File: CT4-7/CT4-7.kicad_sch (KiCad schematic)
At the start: 26 parts

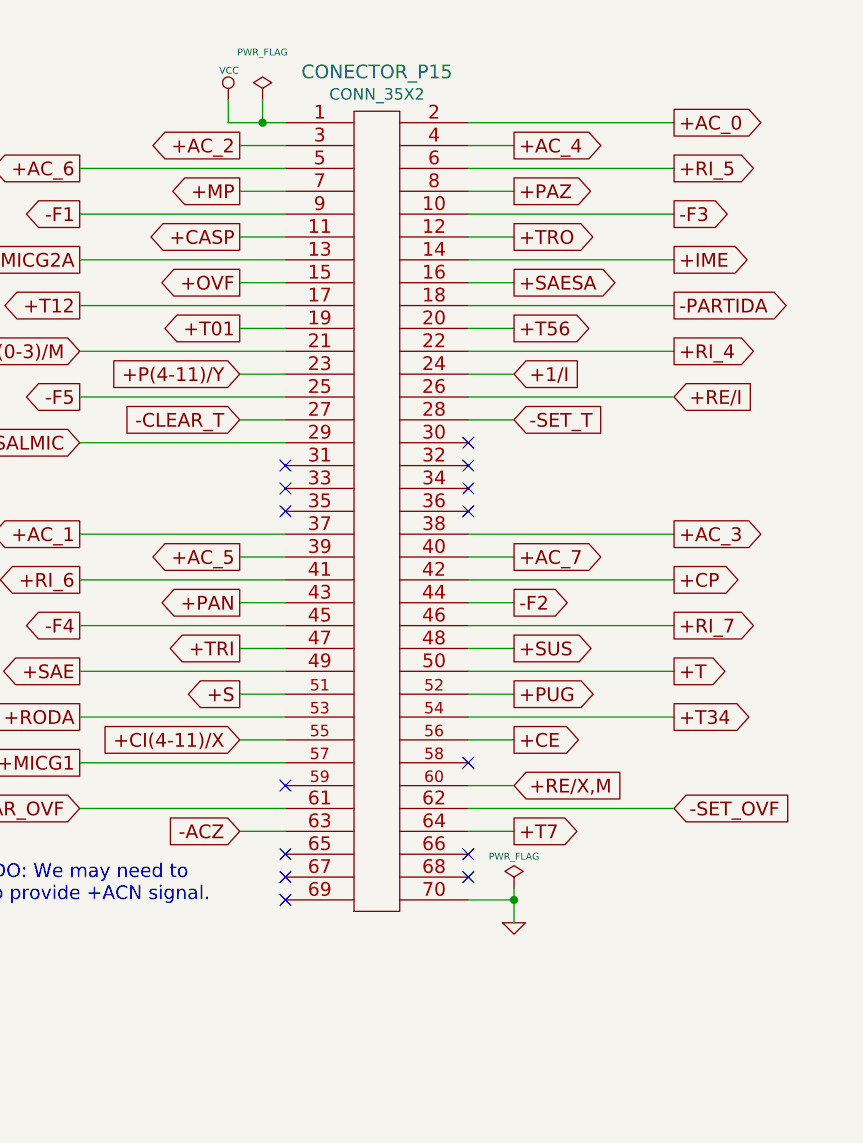
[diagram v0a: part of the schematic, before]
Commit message: cleaning up references
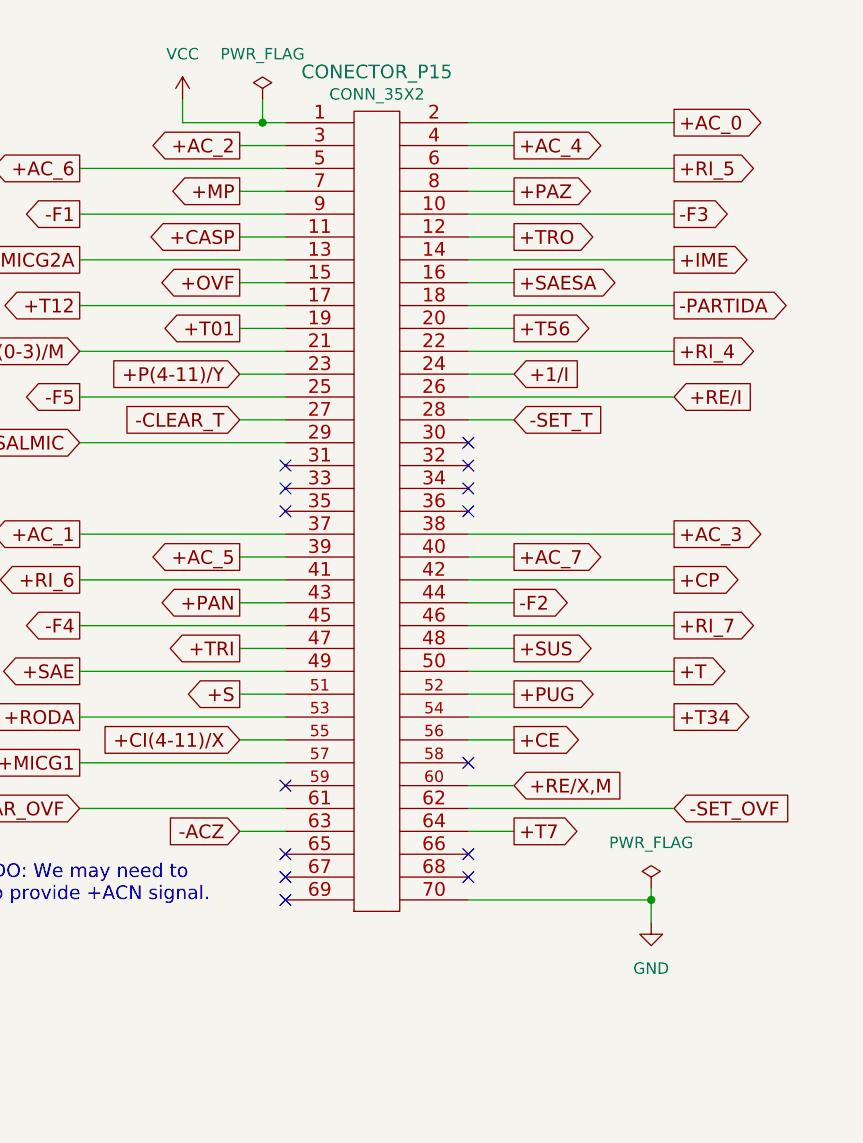
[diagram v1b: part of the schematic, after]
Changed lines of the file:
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@@
 	)
 	(junction
-		(at 472.44 215.9)
+		(at 160.02 213.36)
 		(diameter 0)
 		(color 0 0 0 0)
 	)
 	(junction
-		(at 472.44 210.82)
+		(at 472.44 215.9)
 		(diameter 0)
 		(color 0 0 0 0)
 	)
 	(junction
-		(at 499.11 392.43)
+		(at 472.44 210.82)
 		(diameter 0)
 		(color 0 0 0 0)
 	)
 	(junction
-		(at 538.48 430.53)
+		(at 499.11 392.43)
 		(diameter 0)
 		(color 0 0 0 0)
 	)
 	(junction
-		(at 144.78 213.36)
+		(at 538.48 430.53)
 		(diameter 0)
 		(color 0 0 0 0)
@@
 	(wire
 		(pts
-			(xy 139.7 213.36) (xy 144.78 213.36)
+			(xy 139.7 213.36) (xy 160.02 213.36)
 		)
 		(stroke
@@
 	(wire
 		(pts
-			(xy 144.78 212.09) (xy 144.78 213.36)
+			(xy 160.02 212.09) (xy 160.02 213.36)
 		)
 		(stroke
@@
 	(wire
 		(pts
-			(xy 113.03 127) (xy 116.84 127)
+			(xy 107.95 127) (xy 116.84 127)
 		)
 		(stroke
@@
 	(wire
 		(pts
-			(xy 144.78 213.36) (xy 144.78 215.9)
+			(xy 160.02 213.36) (xy 160.02 215.9)
 		)
 		(stroke
@@
 	(wire
 		(pts
-			(xy 113.03 127) (xy 113.03 124.46)
+			(xy 107.95 127) (xy 107.95 124.46)
 		)
 		(stroke
@@
 	)
 	(symbol
-		(lib_id "CT4-7-rescue:PWR_FLAG-power")
-		(at 116.84 124.46 0)
+		(lib_id "power:GND")
+		(at 160.02 215.9 0)
 		(unit 1)
 		(body_style 1)
@@
 		(in_pos_files yes)
 		(dnp no)
-		(property "Reference" "#FLG01"
-			(at 116.84 122.047 0)
+		(fields_autoplaced yes)
+		(property "Reference" "#PWR0137"
+			(at 160.02 222.25 0)
 			(hide yes)
 			(show_name no)
@@
 			(effects
 				(font
-					(size 0.762 0.762)
+					(size 1.27 1.27)
 				)
 			)
 		)
-		(property "Value" "PWR_FLAG"
-			(at 116.84 119.1768 0)
+		(property "Value" "GND"
+			(at 160.02 220.98 0)
 			(show_name no)
 			(do_not_autoplace no)
 			(effects
 				(font
-					(size 0.762 0.762)
+					(size 1.27 1.27)
 				)
 			)
 		)
 		(property "Footprint" ""
-			(at 116.84 124.46 0)
+			(at 160.02 215.9 0)
 			(hide yes)
 			(show_name no)
@@
 			(effects
 				(font
-					(size 1.524 1.524)
+					(size 1.27 1.27)
 				)
 			)
 		)
 		(property "Datasheet" ""
-			(at 116.84 124.46 0)
+			(at 160.02 215.9 0)
 			(hide yes)
 			(show_name no)
@@
 			(effects
 				(font
-					(size 1.524 1.524)
+					(size 1.27 1.27)
 				)
 			)
 		)
-		(property "Description" ""
-			(at 116.84 124.46 0)
+		(property "Description" "Power symbol creates a global label with name \"GND\" , ground"
+			(at 160.02 215.9 0)
+			(hide yes)
 			(show_name no)
 			(do_not_autoplace no)
@@
 		)
 		(instances
-			(project ""
-				(path "/91180d67-5efd-47f3-b787-983030024d4a"
-					(reference "#FLG01")
-					(unit 1)
-				)
-			)
 			(project "patinhofeio"
 				(path "/aca06203-542d-4682-a7e3-8839e24cce95/20195246-952b-457f-8d3f-2119f4e5893d"
-					(reference "#FLG01")
+					(reference "#PWR0137")
 					(unit 1)
 				)
@@
 	)
 	(symbol
-		(lib_id "CT4-7-rescue:VCC-power")
-		(at 113.03 124.46 0)
+		(lib_id "power:PWR_FLAG")
+		(at 116.84 124.46 0)
 		(unit 1)
 		(body_style 1)
@@
 		(in_pos_files yes)
 		(dnp no)
-		(property "Reference" "#PWR02"
-			(at 113.03 121.92 0)
+		(fields_autoplaced yes)
+		(property "Reference" "#FLG058"
+			(at 116.84 122.555 0)
 			(hide yes)
 			(show_name no)
@@
 			(effects
 				(font
-					(size 0.762 0.762)
+					(size 1.27 1.27)
 				)
 			)
 		)
-		(property "Value" "VCC"
-			(at 113.1062 121.2088 0)
+		(property "Value" "PWR_FLAG"
+			(at 116.84 119.38 0)
 			(show_name no)
 			(do_not_autoplace no)
 			(effects
 				(font
-					(size 0.762 0.762)
+					(size 1.27 1.27)
 				)
 			)
 		)
 		(property "Footprint" ""
-			(at 113.03 124.46 0)
+			(at 116.84 124.46 0)
 			(hide yes)
 			(show_name no)
@@
 			(effects
 				(font
-					(size 1.524 1.524)
+					(size 1.27 1.27)
 				)
 			)
 		)
 		(property "Datasheet" ""
-			(at 113.03 124.46 0)
+			(at 116.84 124.46 0)
 			(hide yes)
 			(show_name no)
@@
 			(effects
 				(font
-					(size 1.524 1.524)
+					(size 1.27 1.27)
 				)
 			)
 		)
-		(property "Description" ""
-			(at 113.03 124.46 0)
+		(property "Description" "Special symbol for telling ERC where power comes from"
+			(at 116.84 124.46 0)
+			(hide yes)
 			(show_name no)
 			(do_not_autoplace no)
@@
 		)
 		(instances
-			(project ""
-				(path "/91180d67-5efd-47f3-b787-983030024d4a"
-					(reference "#PWR02")
-					(unit 1)
-				)
-			)
 			(project "patinhofeio"
 				(path "/aca06203-542d-4682-a7e3-8839e24cce95/20195246-952b-457f-8d3f-2119f4e5893d"
-					(reference "#PWR02")
+					(reference "#FLG058")
 					(unit 1)
 				)
@@
 	)
 	(symbol
-		(lib_id "CT4-7-rescue:PWR_FLAG-power")
-		(at 144.78 212.09 0)
+		(lib_id "power:VCC")
+		(at 107.95 124.46 0)
 		(unit 1)
 		(body_style 1)
@@
 		(in_pos_files yes)
 		(dnp no)
-		(property "Reference" "#FLG03"
-			(at 144.78 209.677 0)
+		(fields_autoplaced yes)
+		(property "Reference" "#PWR0111"
+			(at 107.95 128.27 0)
 			(hide yes)
 			(show_name no)
@@
 			(effects
 				(font
-					(size 0.762 0.762)
+					(size 1.27 1.27)
 				)
 			)
 		)
-		(property "Value" "PWR_FLAG"
-			(at 144.78 208.534 0)
+		(property "Value" "VCC"
+			(at 107.95 119.38 0)
 			(show_name no)
 			(do_not_autoplace no)
 			(effects
 				(font
-					(size 0.762 0.762)
+					(size 1.27 1.27)
 				)
 			)
 		)
 		(property "Footprint" ""
-			(at 144.78 212.09 0)
+			(at 107.95 124.46 0)
 			(hide yes)
 			(show_name no)
@@
 			(effects
 				(font
-					(size 1.524 1.524)
+					(size 1.27 1.27)
 				)
 			)
 		)
 		(property "Datasheet" ""
-			(at 144.78 212.09 0)
+			(at 107.95 124.46 0)
 			(hide yes)
 			(show_name no)
@@
 			(effects
 				(font
-					(size 1.524 1.524)
+					(size 1.27 1.27)
 				)
 			)
 		)
-		(property "Description" ""
-			(at 144.78 212.09 0)
+		(property "Description" "Power symbol creates a global label with name \"VCC\""
+			(at 107.95 124.46 0)
+			(hide yes)
 			(show_name no)
 			(do_not_autoplace no)
@@
 		)
 		(instances
-			(project ""
-				(path "/91180d67-5efd-47f3-b787-983030024d4a"
-					(reference "#FLG03")
-					(unit 1)
-				)
-			)
 			(project "patinhofeio"
 				(path "/aca06203-542d-4682-a7e3-8839e24cce95/20195246-952b-457f-8d3f-2119f4e5893d"
-					(reference "#FLG03")
+					(reference "#PWR0111")
 					(unit 1)
 				)
@@
 	)
 	(symbol
-		(lib_id "CT4-7-rescue:GND")
-		(at 144.78 215.9 0)
+		(lib_id "power:PWR_FLAG")
+		(at 160.02 212.09 0)
 		(unit 1)
 		(body_style 1)
@@
 		(in_pos_files yes)
 		(dnp no)
-		(property "Reference" "#PWR04"
-			(at 144.78 215.9 0)
+		(fields_autoplaced yes)
+		(property "Reference" "#FLG014"
+			(at 160.02 210.185 0)
 			(hide yes)
 			(show_name no)
@@
 			(effects
 				(font
-					(size 0.762 0.762)
+					(size 1.27 1.27)
 				)
 			)
 		)
-		(property "Value" "GND"
-			(at 144.78 217.678 0)
-			(hide yes)
+		(property "Value" "PWR_FLAG"
+			(at 160.02 207.01 0)
 			(show_name no)
 			(do_not_autoplace no)
 			(effects
 				(font
-					(size 0.762 0.762)
+					(size 1.27 1.27)
 				)
 			)
 		)
 		(property "Footprint" ""
-			(at 144.78 215.9 0)
+			(at 160.02 212.09 0)
 			(hide yes)
 			(show_name no)
@@
 			(effects
 				(font
-					(size 1.524 1.524)
+					(size 1.27 1.27)
 				)
 			)
 		)
 		(property "Datasheet" ""
-			(at 144.78 215.9 0)
+			(at 160.02 212.09 0)
 			(hide yes)
 			(show_name no)
@@
 			(effects
 				(font
-					(size 1.524 1.524)
+					(size 1.27 1.27)
 				)
 			)
 		)
-		(property "Description" ""
-			(at 144.78 215.9 0)
+		(property "Description" "Special symbol for telling ERC where power comes from"
+			(at 160.02 212.09 0)
+			(hide yes)
 			(show_name no)
 			(do_not_autoplace no)
@@
 		)
 		(instances
-			(project ""
-				(path "/91180d67-5efd-47f3-b787-983030024d4a"
-					(reference "#PWR04")
-					(unit 1)
-				)
-			)
 			(project "patinhofeio"
 				(path "/aca06203-542d-4682-a7e3-8839e24cce95/20195246-952b-457f-8d3f-2119f4e5893d"
-					(reference "#PWR04")
+					(reference "#FLG014")
 					(unit 1)
 				)

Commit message: Some initial fixing of ERC errors.
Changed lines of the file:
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@@
 	)
 	(junction
-		(at 160.02 213.36)
-		(diameter 0)
-		(color 0 0 0 0)
-	)
-	(junction
 		(at 472.44 215.9)
 		(diameter 0)
@@
 	)
 	(junction
-		(at 116.84 127)
-		(diameter 0)
-		(color 0 0 0 0)
-	)
-	(junction
 		(at 257.81 273.05)
 		(diameter 0)
@@
 	(wire
 		(pts
-			(xy 160.02 212.09) (xy 160.02 213.36)
-		)
-		(stroke
-			(width 0)
-			(type default)
-		)
-	)
-	(wire
-		(pts
 			(xy 645.16 163.83) (xy 650.24 163.83)
 		)
@@
 	(wire
 		(pts
-			(xy 107.95 127) (xy 116.84 127)
-		)
-		(stroke
-			(width 0)
-			(type default)
-		)
-	)
-	(wire
-		(pts
 			(xy 162.56 127) (xy 139.7 127)
 		)
@@
 	(wire
 		(pts
-			(xy 116.84 124.46) (xy 116.84 127)
-		)
-		(stroke
-			(width 0)
-			(type default)
-		)
-	)
-	(wire
-		(pts
 			(xy 650.24 419.1) (xy 657.86 419.1)
 		)
@@
 	(wire
 		(pts
-			(xy 116.84 127) (xy 119.38 127)
+			(xy 107.95 127) (xy 119.38 127)
 		)
 		(stroke
@@
 	)
 	(symbol
-		(lib_id "power:PWR_FLAG")
-		(at 116.84 124.46 0)
-		(unit 1)
-		(body_style 1)
-		(exclude_from_sim no)
-		(in_bom yes)
-		(on_board yes)
-		(in_pos_files yes)
-		(dnp no)
-		(fields_autoplaced yes)
-		(property "Reference" "#FLG058"
-			(at 116.84 122.555 0)
-			(hide yes)
-			(show_name no)
-			(do_not_autoplace no)
-			(effects
-				(font
-					(size 1.27 1.27)
-				)
-			)
-		)
-		(property "Value" "PWR_FLAG"
-			(at 116.84 119.38 0)
-			(show_name no)
-			(do_not_autoplace no)
-			(effects
-				(font
-					(size 1.27 1.27)
-				)
-			)
-		)
-		(property "Footprint" ""
-			(at 116.84 124.46 0)
-			(hide yes)
-			(show_name no)
-			(do_not_autoplace no)
-			(effects
-				(font
-					(size 1.27 1.27)
-				)
-			)
-		)
-		(property "Datasheet" ""
-			(at 116.84 124.46 0)
-			(hide yes)
-			(show_name no)
-			(do_not_autoplace no)
-			(effects
-				(font
-					(size 1.27 1.27)
-				)
-			)
-		)
-		(property "Description" "Special symbol for telling ERC where power comes from"
-			(at 116.84 124.46 0)
-			(hide yes)
-			(show_name no)
-			(do_not_autoplace no)
-			(effects
-				(font
-					(size 1.27 1.27)
-				)
-			)
-		)
-		(pin "1"
-		)
-		(instances
-			(project "patinhofeio"
-				(path "/aca06203-542d-4682-a7e3-8839e24cce95/20195246-952b-457f-8d3f-2119f4e5893d"
-					(reference "#FLG058")
-					(unit 1)
-				)
-			)
-		)
-	)
-	(symbol
 		(lib_id "power:VCC")
 		(at 107.95 124.46 0)
@@
 					(unit 1)
 				)
-			)
-		)
-	)
-	(symbol
-		(lib_id "power:PWR_FLAG")
-		(at 160.02 212.09 0)
-		(unit 1)
-		(body_style 1)
-		(exclude_from_sim no)
-		(in_bom yes)
-		(on_board yes)
-		(in_pos_files yes)
-		(dnp no)
-		(fields_autoplaced yes)
-		(property "Reference" "#FLG014"
-			(at 160.02 210.185 0)
-			(hide yes)
-			(show_name no)
-			(do_not_autoplace no)
-			(effects
-				(font
-					(size 1.27 1.27)
-				)
-			)
-		)
-		(property "Value" "PWR_FLAG"
-			(at 160.02 207.01 0)
-			(show_name no)
-			(do_not_autoplace no)
-			(effects
-				(font
-					(size 1.27 1.27)
-				)
-			)
-		)
-		(property "Footprint" ""
-			(at 160.02 212.09 0)
-			(hide yes)
-			(show_name no)
-			(do_not_autoplace no)
-			(effects
-				(font
-					(size 1.27 1.27)
-				)
-			)
-		)
-		(property "Datasheet" ""
-			(at 160.02 212.09 0)
-			(hide yes)
-			(show_name no)
-			(do_not_autoplace no)
-			(effects
-				(font
-					(size 1.27 1.27)
-				)
-			)
-		)
-		(property "Description" "Special symbol for telling ERC where power comes from"
-			(at 160.02 212.09 0)
-			(hide yes)
-			(show_name no)
-			(do_not_autoplace no)
-			(effects
-				(font
-					(size 1.27 1.27)
-				)
-			)
-		)
-		(pin "1"
-		)
-		(instances
-			(project "patinhofeio"
-				(path "/aca06203-542d-4682-a7e3-8839e24cce95/20195246-952b-457f-8d3f-2119f4e5893d"
-					(reference "#FLG014")
-					(unit 1)
-				)

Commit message: fixing a whole bunch more ERC errors
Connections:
- net -RI_5: no longer 1C_P15.5, 2A_P15.6, 4E_P15.6
- new net -RD_5: 1C_P15.5, 2A_P15.6, 4E_P15.6
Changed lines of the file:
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@@
 		)
 	)
+	(label "-RI_6"
+		(at 461.01 430.53 180)
+		(effects
+			(font
+				(size 1.524 1.524)
+			)
+			(justify right bottom)
+		)
+	)
+	(label "-RD_5"
+		(at 461.01 405.13 180)
+		(effects
+			(font
+				(size 1.524 1.524)
+			)
+			(justify right bottom)
+		)
+	)
+	(label "-RD_5"
+		(at 228.6 146.05 180)
+		(effects
+			(font
+				(size 1.524 1.524)
+			)
+			(justify right bottom)
+		)
+	)
+	(label "-RD_5"
+		(at 304.8 406.4 0)
+		(effects
+			(font
+				(size 1.524 1.524)
+			)
+			(justify left bottom)
+		)
+	)
+	(label "-RI_6"
+		(at 304.8 425.45 0)
+		(effects
+			(font
+				(size 1.524 1.524)
+			)
+			(justify left bottom)
+		)
+	)
+	(label "-RI_6"
+		(at 330.2 146.05 180)
+		(effects
+			(font
+				(size 1.524 1.524)
+			)
+			(justify right bottom)
+		)
+	)
 	(global_label "+AC_4"
 		(shape input)
@@
 		)
 	)
-	(global_label "-RI_6"
-		(shape input)
-		(at 461.01 430.53 180)
-		(effects
-			(font
-				(size 1.524 1.524)
-			)
-			(justify right)
-		)
-		(property "Intersheetrefs" "${INTERSHEET_REFS}"
-			(at 461.01 430.53 0)
-			(hide yes)
-			(show_name no)
-			(do_not_autoplace no)
-			(effects
-				(font
-					(size 1.27 1.27)
-				)
-			)
-		)
-	)
 	(global_label "-RI_5"
 		(shape input)
@@
 		)
 	)
-	(global_label "-RI_5"
-		(shape input)
-		(at 228.6 146.05 180)
-		(effects
-			(font
-				(size 1.524 1.524)
-			)
-			(justify right)
-		)
-		(property "Intersheetrefs" "${INTERSHEET_REFS}"
-			(at 228.6 146.05 0)
-			(hide yes)
-			(show_name no)
-			(do_not_autoplace no)
-			(effects
-				(font
-					(size 1.27 1.27)
-				)
-			)
-		)
-	)
 	(global_label "-SAE"
 		(shape input)
@@
 		)
 	)
-	(global_label "-RI_5"
-		(shape output)
-		(at 304.8 406.4 0)
-		(effects
-			(font
-				(size 1.524 1.524)
-			)
-			(justify left)
-		)
-		(property "Intersheetrefs" "${INTERSHEET_REFS}"
-			(at 304.8 406.4 0)
-			(hide yes)
-			(show_name no)
-			(do_not_autoplace no)
-			(effects
-				(font
-					(size 1.27 1.27)
-				)
-			)
-		)
-	)
 	(global_label "+T56"
 		(shape input)
@@
 		)
 	)
-	(global_label "-RI_6"
-		(shape input)
-		(at 330.2 146.05 180)
-		(effects
-			(font
-				(size 1.524 1.524)
-			)
-			(justify right)
-		)
-		(property "Intersheetrefs" "${INTERSHEET_REFS}"
-			(at 330.2 146.05 0)
-			(hide yes)
-			(show_name no)
-			(do_not_autoplace no)
-			(effects
-				(font
-					(size 1.27 1.27)
-				)
-			)
-		)
-	)
 	(global_label "-AC_2"
 		(shape input)
@@
 		)
 	)
-	(global_label "-RI_6"
-		(shape output)
-		(at 304.8 425.45 0)
-		(effects
-			(font
-				(size 1.524 1.524)
-			)
-			(justify left)
-		)
-		(property "Intersheetrefs" "${INTERSHEET_REFS}"
-			(at 304.8 425.45 0)
-			(hide yes)
-			(show_name no)
-			(do_not_autoplace no)
-			(effects
-				(font
-					(size 1.27 1.27)
-				)
-			)
-		)
-	)
 	(global_label "+T12"
 		(shape output)
@@
 			(hide yes)
 			(show_name no)
-			(do_not_autoplace no)
-			(effects
-				(font
-					(size 1.27 1.27)
-				)
-			)
-		)
-	)
-	(global_label "-RI_5"
-		(shape input)
-		(at 461.01 405.13 180)
-		(effects
-			(font
-				(size 1.524 1.524)
-			)
-			(justify right)
-		)
-		(property "Intersheetrefs" "${INTERSHEET_REFS}"
-			(at 461.01 405.13 0)
-			(hide yes)
-			(show_name no)

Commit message: melhorias dessa semana
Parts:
- removed 1C_P15, 1D_P15, 2B_P15, 2E_P15, 3C_P15, 4D_P15, 5B_P15, 5C_P15: 7400, symbol CT4-7-rescue:7400
- added 1C_P15, 1D_P15, 2B_P15, 2E_P15, 3C_P15, 4D_P15, 5B_P15, 5C_P15: 74LS00, symbol 74xx:74LS00
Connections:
- net +(F3+F4): now also 2E_P15.8, 4D_P15.9, 5B_P15.9, 5C_P15.1
- net +(PARTIDA.(-RODA)): now also 2E_P15.12
- net +(TRO+TRI): now also 2B_P15.11, 3C_P15.10, 5C_P15.2
- net +CI(0-3)/M: now also 2E_P15.6
- net +CI(4-11)/X: now also 2E_P15.3
- net +F2: now also 1C_P15.12, 3C_P15.2
- net +F3: now also 3C_P15.4
- net +F4: now also 3C_P15.9
- net +OVF: now also 1C_P15.4
- net +P(4-11)/Y: now also 5B_P15.6
- net +PAN: now also 2B_P15.4
- net +PAZ: now also 2B_P15.2
- net +PUG: now also 4D_P15.10
- net +RI_5: now also 1C_P15.2
- net +RI_6: now also 1D_P15.1, 4D_P15.2
- net +RI_7: now also 4D_P15.1, 4D_P15.5
- net +SAESA: now also 1C_P15.13
- net +SALMIC: now also 1D_P15.8
- net +T: now also 1C_P15.1
- net +TRO: now also 5B_P15.10
- net -(F4.(TRO+TRI)): now also 3C_P15.8
- net -ACZ: now also 2B_P15.1
- net -AC_0: now also 2B_P15.5
- net -CASP: now also 2B_P15.10
- net -CE: now also 5B_P15.1
- net -CP: now also 3C_P15.13, 5B_P15.2
- net -F1: now also 1D_P15.12
- net -F2: now also 1D_P15.13
- net -F3: now also 2E_P15.9
- net -F4: now also 2E_P15.10
- net -F5: now also 4D_P15.13, 5C_P15.5
- net -MP: now also 3C_P15.12
- net -RD_5: now also 1C_P15.5
- net -RI_6: now also 1D_P15.5, 4D_P15.4
- net -SUS: now also 2B_P15.9
- net -TRI: now also 2B_P15.13
- net -TRO: now also 2B_P15.12
- net GND: now also 1C_P15.7 (GND), 1D_P15.7 (GND), 2B_P15.7 (GND), 2E_P15.7 (GND), 3C_P15.7 (GND), 4D_P15.7 (GND), 5B_P15.7 (GND), 5C_P15.7 (GND)
- net VCC: now also 1C_P15.14 (VCC), 1D_P15.14 (VCC), 2B_P15.14 (VCC), 2E_P15.14 (VCC), 3C_P15.14 (VCC), 4D_P15.14 (VCC), 5B_P15.14 (VCC), 5C_P15.14 (VCC)
- net at 5D_P15.3, 5D_P15.4, 5D_P15.5: now also 5C_P15.6
- net at 3B_P15.1: now also 1C_P15.8, 1D_P15.2
- net at 3B_P15.2: now also 1D_P15.4
- net at 5A_P15.6: now also 5B_P15.5
- net at 3D_P15.10: now also 5B_P15.3
- net at 3D_P15.8: now also 5B_P15.4
- net at 3B_P15.13: now also 5B_P15.8
- net at 4C_P15.2: now also 4D_P15.11
- net at 4E_P15.11, 4E_P15.9: now also 4D_P15.6
- net at 4E_P15.3, 4E_P15.5: now also 4D_P15.3
- net at 3D_P15.6: now also 2E_P15.5
- net at 1E_P15.8, 3D_P15.12: now also 2E_P15.1, 2E_P15.2, 2E_P15.4
- net at 1E_P15.1: now also 1D_P15.11
- net at 2D_P15.1: now also 2B_P15.3
- net at 2C_P15.4: now also 1C_P15.11
- net at 3B_P15.3: now also 2E_P15.11
- net at 2D_P15.4: now also 2B_P15.6
- net at 2D_P15.6: now also 3C_P15.1
- net at 2D_P15.10: now also 3C_P15.3
- net at 2D_P15.12: now also 3C_P15.6
- new net: 2E_P15.13, 3C_P15.11
- new net: 2B_P15.8, 3C_P15.5
- new net: 1D_P15.3, 1D_P15.9
- new net: 1C_P15.3, 1C_P15.9
- new net: 1C_P15.10, 1C_P15.6
- new net: 1D_P15.10, 1D_P15.6
- new net: 5C_P15.3, 5C_P15.4
- new net: 4D_P15.12, 4D_P15.8
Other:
- moved on the sheet: 5D_P15B
